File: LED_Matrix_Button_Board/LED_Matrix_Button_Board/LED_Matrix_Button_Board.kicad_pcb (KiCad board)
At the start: 2 copper layers, 74.3 x 21 mm, 11 parts, among them J1 Buttons, SW1 Ok, SW2 Back, SW3 F1, SW4 F2, SW5 F3, SW6 F4

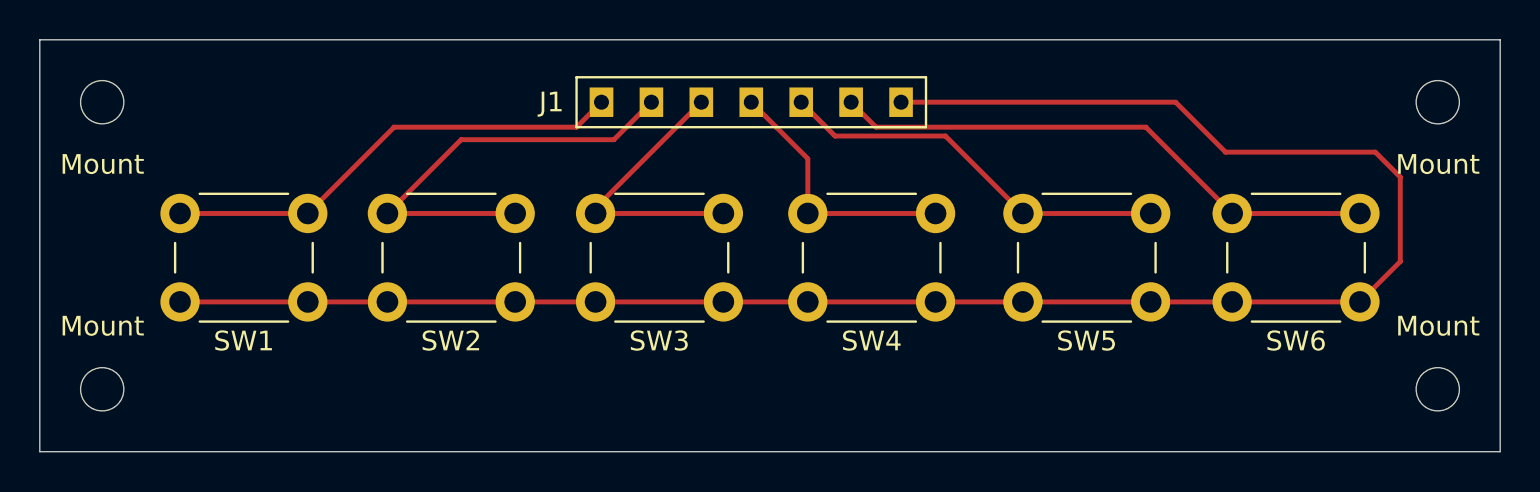
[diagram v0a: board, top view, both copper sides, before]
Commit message: Created Gerber plots of new driver board design, button board, and new LED board As of 12/15/2023, all three PCBs have been submitted to JLCPCB for manufacturing.
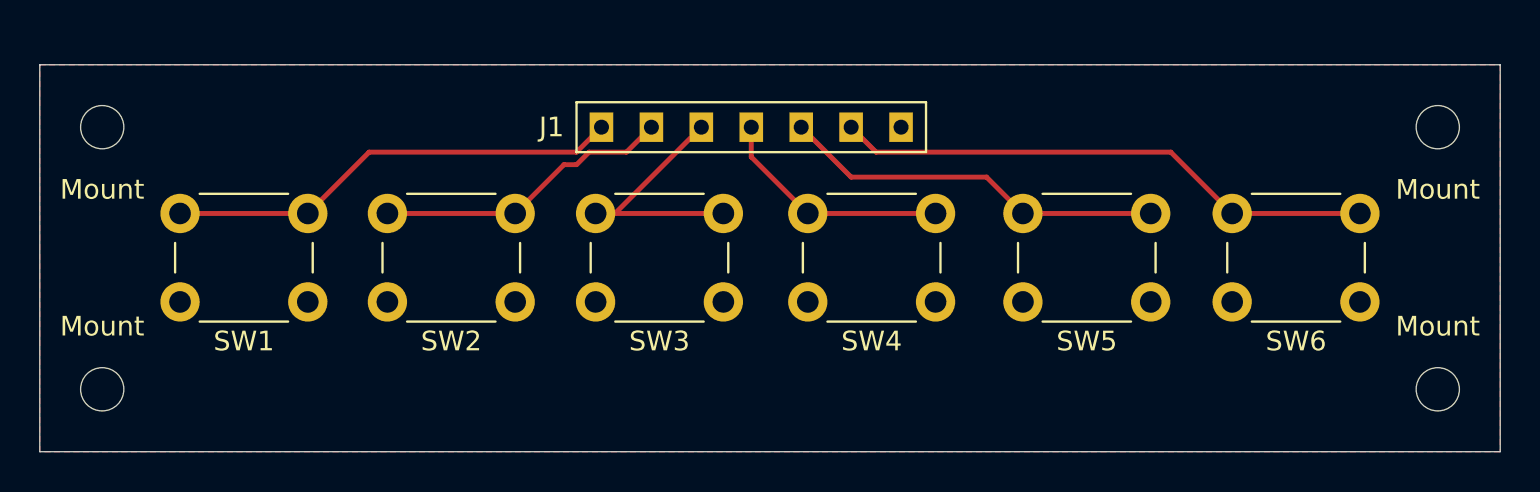
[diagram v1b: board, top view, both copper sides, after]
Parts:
- moved J1 1.27 mm to (142.2, 103.5)
- moved Mount 1.27 mm to (186.7, 103.5)
- moved Mount 1.27 mm to (118.7, 103.5)
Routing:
- net Net-(J1-Pad7): track 94.2 -> 0.00 mm
- net Net-(J1-Pad2): track 22.3 -> 15.2 mm
- net Net-(J1-Pad4): track 13.4 -> 12.1 mm
- net Net-(J1-Pad1): track 23.8 -> 23.3 mm
- net Net-(J1-Pad5): track 20.1 -> 19.6 mm
- net Net-(J1-Pad6): track 28.2 -> 27.7 mm
- added copper zone on F.Cu, net Net-(J1-Pad7)
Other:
- board size 74.3 x 21 mm -> 74.3 x 19.7 mm
